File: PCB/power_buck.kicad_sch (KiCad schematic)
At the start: 6 parts

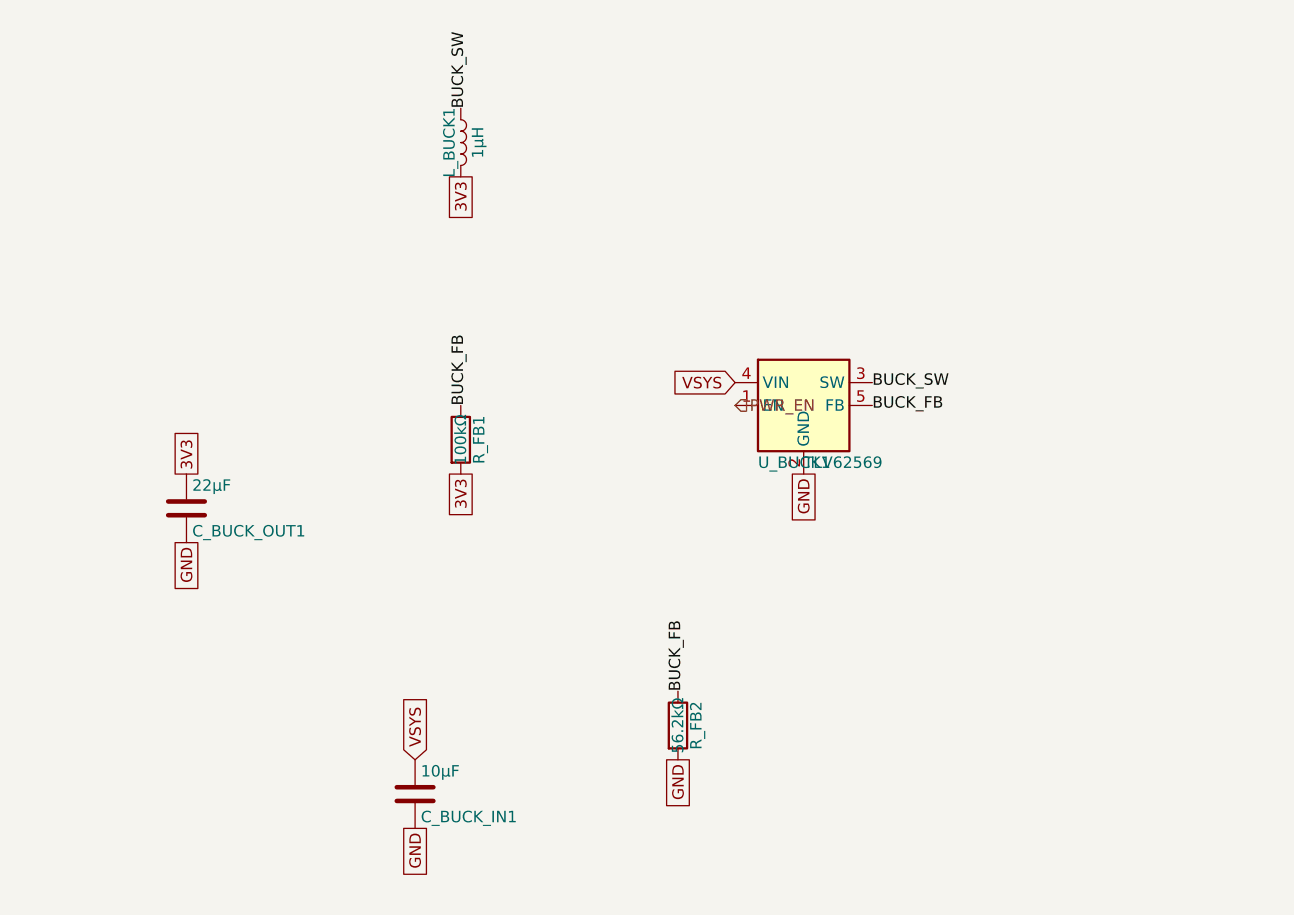
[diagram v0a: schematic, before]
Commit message: Fix footprints and begin layout (#17)
* refactor: updated gulikit footprint

This updates the gulikit thumbstick footprint to be accurate.

* layout: beginning pcb layout

This updates the schematic with a few different footprints while also starts the layout.
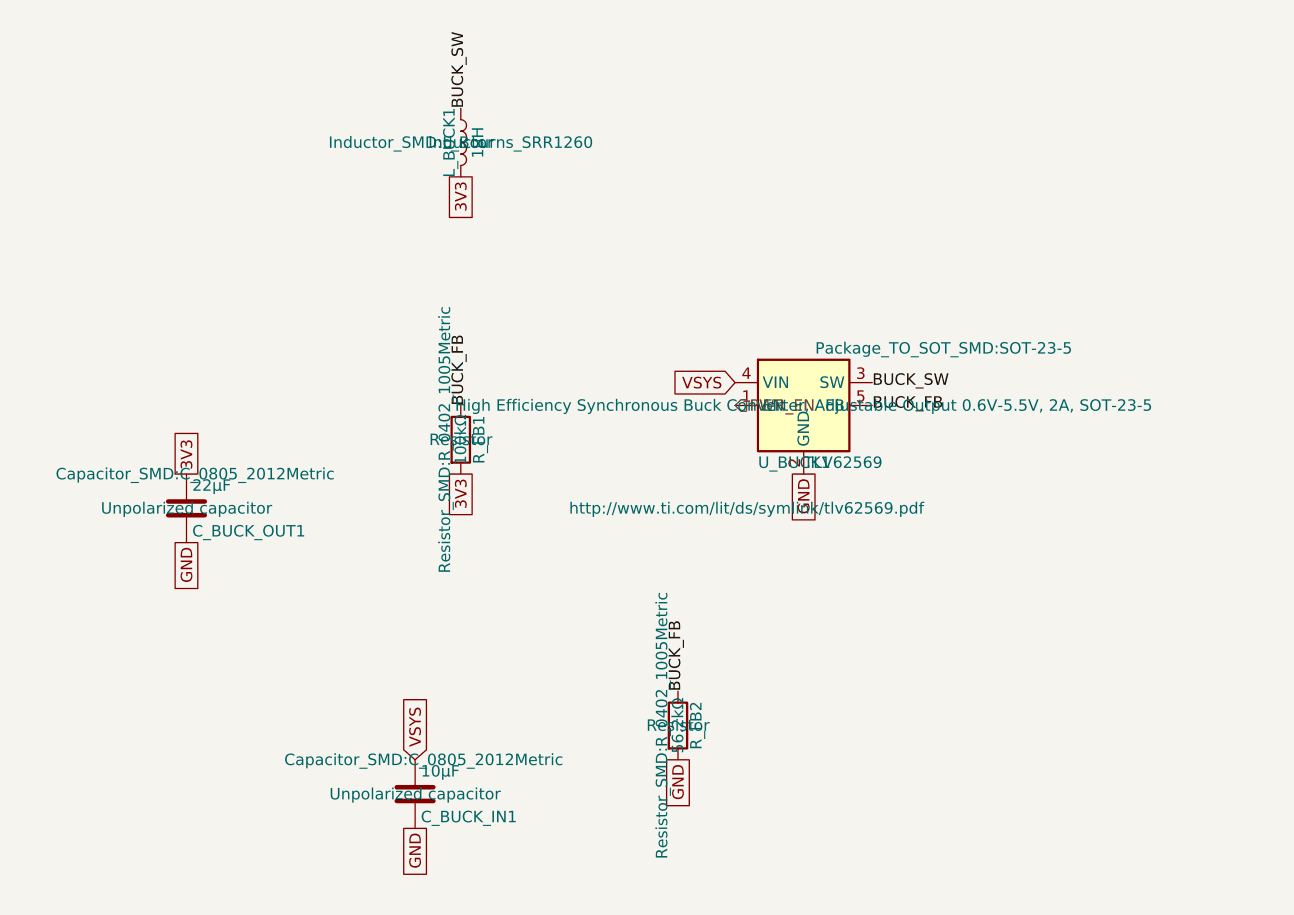
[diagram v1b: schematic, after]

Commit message: refactor: swap footprints and add symmetry
This updates the footprints of a couple components to be smaller and closer to what we want. It also adds two buttons to ensure left and right side symmetry.
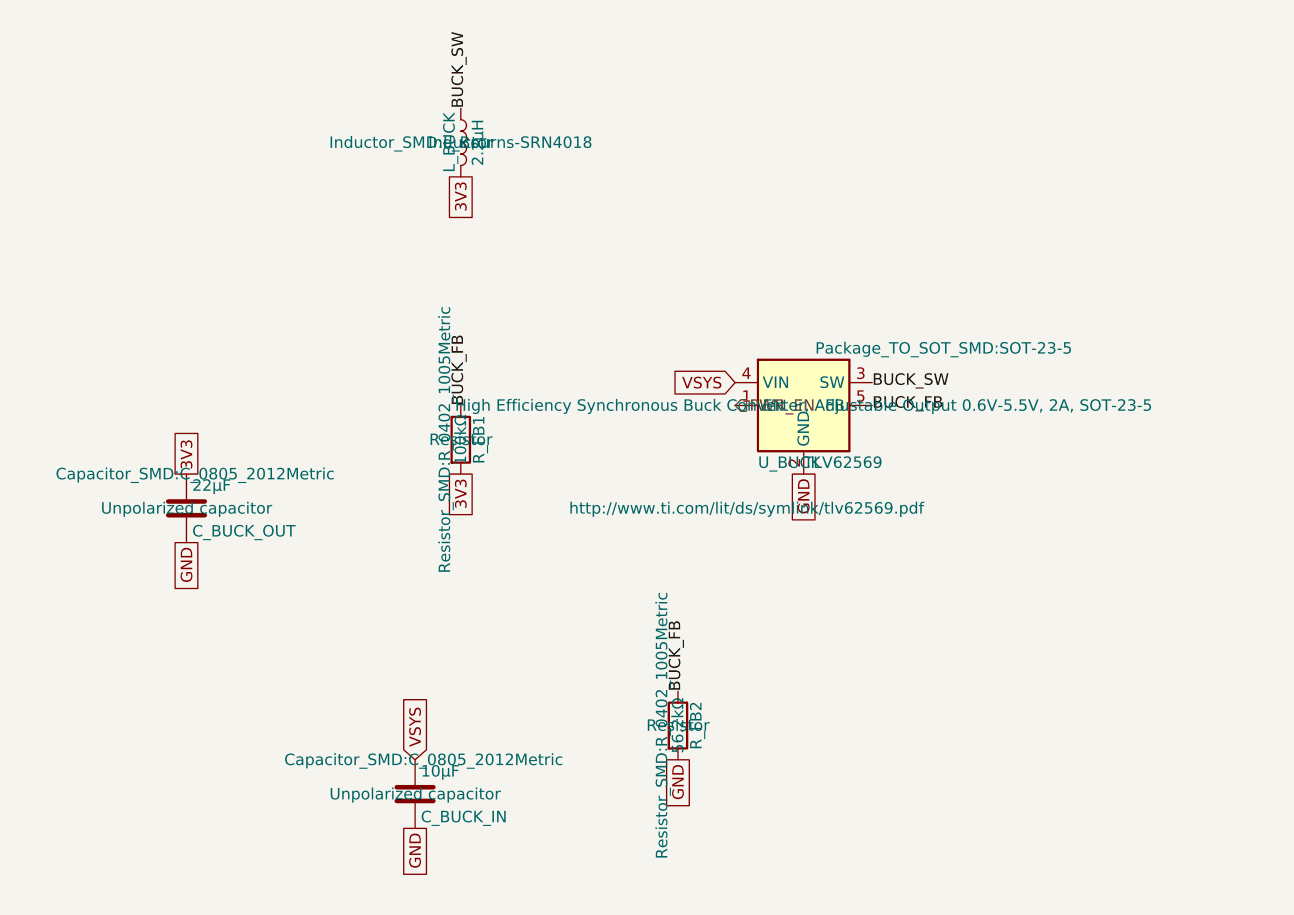
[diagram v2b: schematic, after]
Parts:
- removed C_BUCK_IN1: 10µF, Capacitor_SMD:C_0805_2012Metric, symbol Device:C
- removed C_BUCK_OUT1: 22µF, Capacitor_SMD:C_0805_2012Metric, symbol Device:C
- removed L_BUCK1: 1µH, Inductor_SMD:L_Bourns_SRR1260, symbol Device:L
- removed U_BUCK1: TLV62569, Package_TO_SOT_SMD:SOT-23-5, symbol Regulator_Switching:TLV62569DBV
- added C_BUCK_IN: 10µF, Capacitor_SMD:C_0805_2012Metric, symbol Device:C
- added C_BUCK_OUT: 22µF, Capacitor_SMD:C_0805_2012Metric, symbol Device:C
- added L_BUCK: 2.2µH, Inductor_SMD:L_Bourns-SRN4018, symbol Device:L
- added U_BUCK: TLV62569, Package_TO_SOT_SMD:SOT-23-5, symbol Regulator_Switching:TLV62569DBV
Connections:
- net 3V3: now also C_BUCK_OUT.1, L_BUCK.2
- net BUCK_FB: now also U_BUCK.5 (FB)
- net BUCK_SW: now also L_BUCK.1, U_BUCK.3 (SW)
- net GND: now also C_BUCK_IN.2, C_BUCK_OUT.2, U_BUCK.2 (GND)
- net PWR_EN: now also U_BUCK.1 (EN)
- net VSYS: now also C_BUCK_IN.1, U_BUCK.4 (VIN)

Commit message: layout: everything is on the board
The board edge cuts are down to 100mm x 35mm. All the components have the right footprints and are on the board, but no traces exist yet, and not all circuits are laid out properly yet. Lots of DRC warnings.
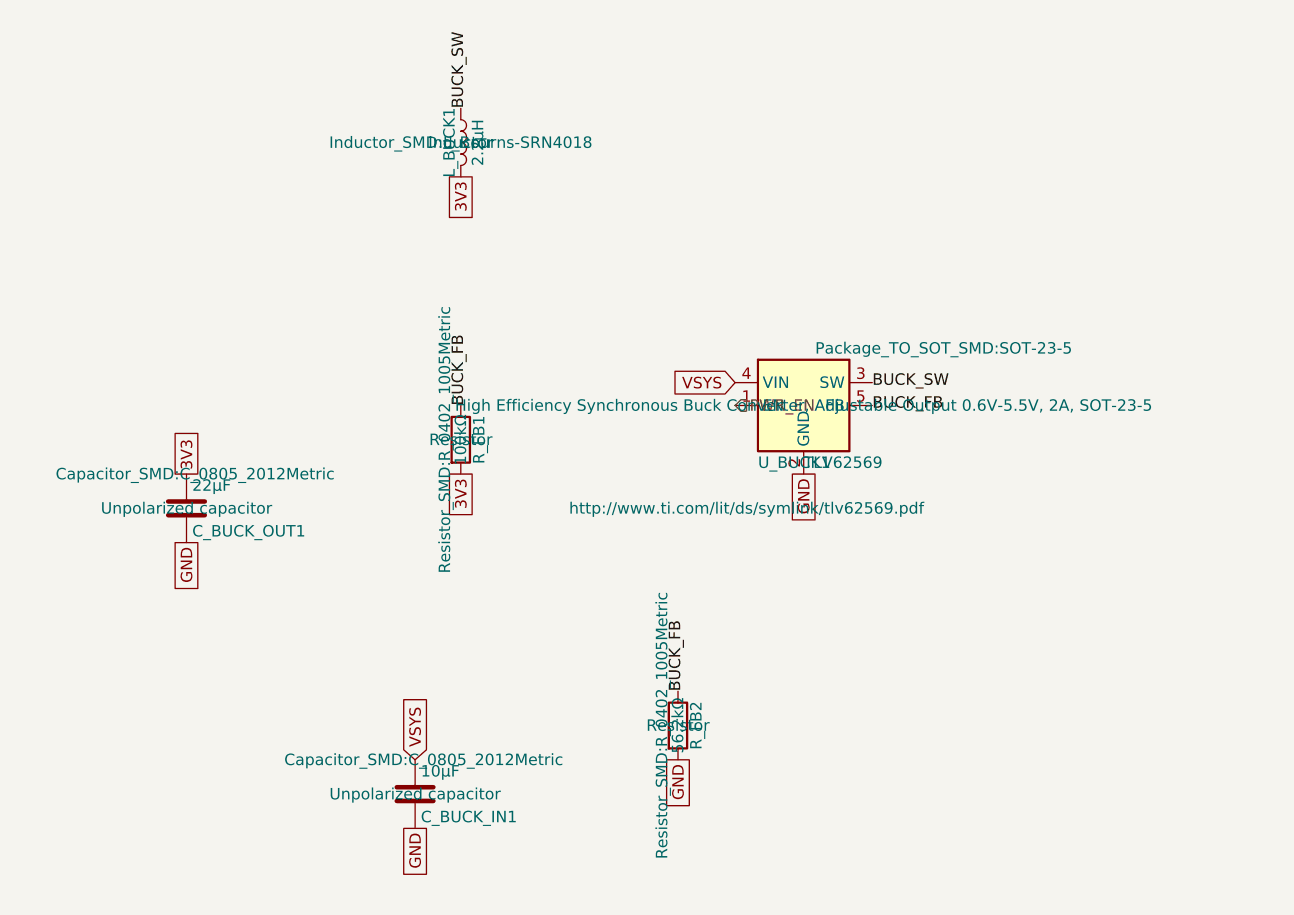
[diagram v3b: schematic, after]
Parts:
- removed C_BUCK_IN: 10µF, Capacitor_SMD:C_0805_2012Metric, symbol Device:C
- removed C_BUCK_OUT: 22µF, Capacitor_SMD:C_0805_2012Metric, symbol Device:C
- removed L_BUCK: 2.2µH, Inductor_SMD:L_Bourns-SRN4018, symbol Device:L
- removed U_BUCK: TLV62569, Package_TO_SOT_SMD:SOT-23-5, symbol Regulator_Switching:TLV62569DBV
- added C_BUCK_IN1: 10µF, Capacitor_SMD:C_0805_2012Metric, symbol Device:C
- added C_BUCK_OUT1: 22µF, Capacitor_SMD:C_0805_2012Metric, symbol Device:C
- added L_BUCK1: 2.2µH, Inductor_SMD:L_Bourns-SRN4018, symbol Device:L
- added U_BUCK1: TLV62569, Package_TO_SOT_SMD:SOT-23-5, symbol Regulator_Switching:TLV62569DBV
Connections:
- net 3V3: now also C_BUCK_OUT1.1, L_BUCK1.2
- net BUCK_FB: now also U_BUCK1.5 (FB)
- net BUCK_SW: now also L_BUCK1.1, U_BUCK1.3 (SW)
- net GND: now also C_BUCK_IN1.2, C_BUCK_OUT1.2, U_BUCK1.2 (GND)
- net PWR_EN: now also U_BUCK1.1 (EN)
- net VSYS: now also C_BUCK_IN1.1, U_BUCK1.4 (VIN)

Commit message: task: first validation pass
This is the results post first kicad-happy run.
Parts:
- R_FB1: value 100kΩ -> 255kΩ
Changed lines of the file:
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@@
 			)
 		)
-		(property "Value" "100kΩ"
+		(property "Value" "255kΩ"
 			(at 144.78 101.6 90)
 			(show_name no)

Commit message: task: part number populated (#26)
kicad-happy run part 2 - MPN numbers populated
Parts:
- C_BUCK_IN1: MF (none) -> Yageo; Manufacturer_Part_Number (none) -> CC0805KRX5R7BB106
- C_BUCK_OUT1: MF (none) -> Yageo; Manufacturer_Part_Number (none) -> CC0805KRX5R7BB226
- L_BUCK1: MF (none) -> Bourns; Manufacturer_Part_Number (none) -> SRN4018-2R2M
- R_FB1: MF (none) -> Yageo; Manufacturer_Part_Number (none) -> RC0402FR-07255KL
- R_FB2: MF (none) -> Yageo; Manufacturer_Part_Number (none) -> RC0402FR-0756K2L
- U_BUCK1: MF (none) -> Texas Instruments; Manufacturer_Part_Number (none) -> TLV62569DBV
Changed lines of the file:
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@@
+			)
+		)
+		(property "MF" "Yageo" (at 0 0 0)
+			(effects
+				(font
+					(size 1.27 1.27)
+				)
+				(hide yes)
+			)
+		)
+		(property "Manufacturer_Part_Number" "RC0402FR-07255KL" (at 0 0 0)
+			(effects
+				(font
+					(size 1.27 1.27)
+				)
+				(hide yes)
 			)
 		)
@@
 			)
 		)
+		(property "MF" "Bourns" (at 0 0 0)
+			(effects
+				(font
+					(size 1.27 1.27)
+				)
+				(hide yes)
+			)
+		)
+		(property "Manufacturer_Part_Number" "SRN4018-2R2M" (at 0 0 0)
+			(effects
+				(font
+					(size 1.27 1.27)
+				)
+				(hide yes)
+			)
+		)
 		(pin "1"
 		)
@@
 			)
 		)
+		(property "MF" "Texas Instruments" (at 0 0 0)
+			(effects
+				(font
+					(size 1.27 1.27)
+				)
+				(hide yes)
+			)
+		)
+		(property "Manufacturer_Part_Number" "TLV62569DBV" (at 0 0 0)
+			(effects
+				(font
+					(size 1.27 1.27)
+				)
+				(hide yes)
+			)
+		)
 		(pin "1"
 		)
@@
 			)
 		)
+		(property "MF" "Yageo" (at 0 0 0)
+			(effects
+				(font
+					(size 1.27 1.27)
+				)
+				(hide yes)
+			)
+		)
+		(property "Manufacturer_Part_Number" "CC0805KRX5R7BB106" (at 0 0 0)
+			(effects
+				(font
+					(size 1.27 1.27)
+				)
+				(hide yes)
+			)
+		)
 		(pin "1"
 		)
@@
 			)
 		)
+		(property "MF" "Yageo" (at 0 0 0)
+			(effects
+				(font
+					(size 1.27 1.27)
+				)
+				(hide yes)
+			)
+		)
+		(property "Manufacturer_Part_Number" "CC0805KRX5R7BB226" (at 0 0 0)
+			(effects
+				(font
+					(size 1.27 1.27)
+				)
+				(hide yes)
+			)
+		)
 		(pin "1"
 		)
@@
 			)
 		)
+		(property "MF" "Yageo" (at 0 0 0)
+			(effects
+				(font
+					(size 1.27 1.27)
+				)
+				(hide yes)
+			)
+		)
+		(property "Manufacturer_Part_Number" "RC0402FR-0756K2L" (at 0 0 0)
+			(effects
+				(font
+					(size 1.27 1.27)
+				)
+				(hide yes)
+			)
+		)

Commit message: task: more gerbers
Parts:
- U_BUCK1: Manufacturer_Part_Number TLV62569DBV -> TLV62569DBVR
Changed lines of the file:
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@@
 			)
 		)
-		(property "Manufacturer_Part_Number" "TLV62569DBV"
+		(property "Manufacturer_Part_Number" "TLV62569DBVR"
 			(at 0 0 0)
 			(hide yes)
